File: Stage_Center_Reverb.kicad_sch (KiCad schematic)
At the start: 47 parts, among them J1 Input, J10 Power, J2 Output, J3 Tank, SW1a1 SW_SPDT, SW1c1 SW_SPDT, SW2 kill, U1 TL072, U10 L78L15, U11 L79L15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

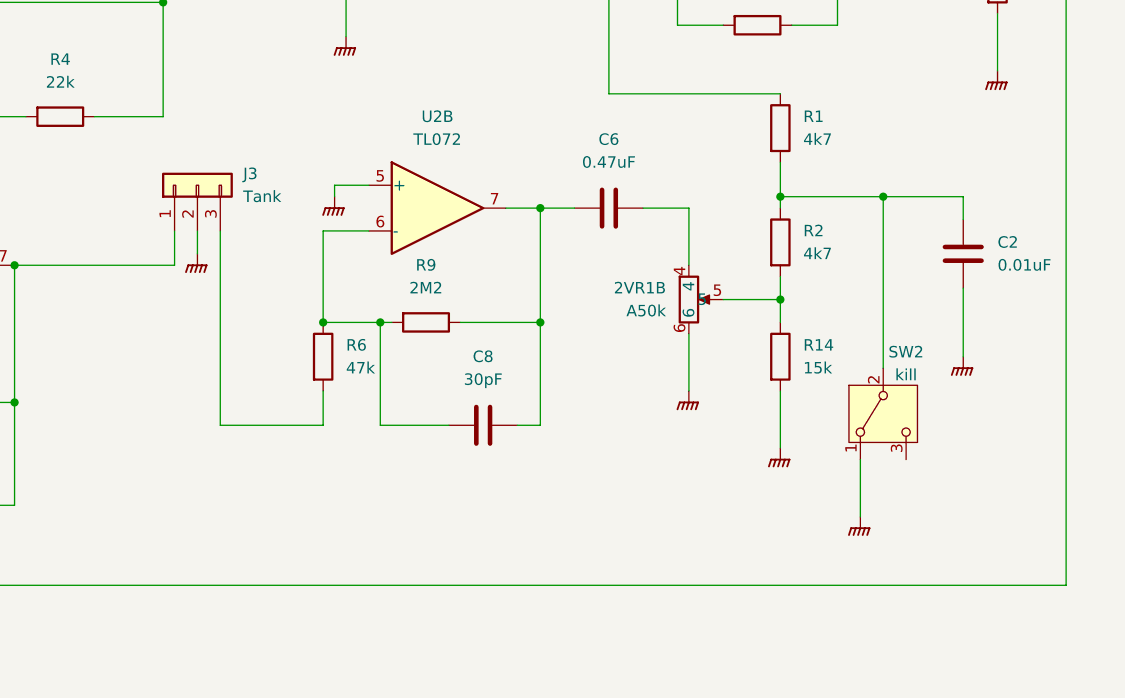
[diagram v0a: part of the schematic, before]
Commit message: 全体ではなく外周をGNDで囲むように変更
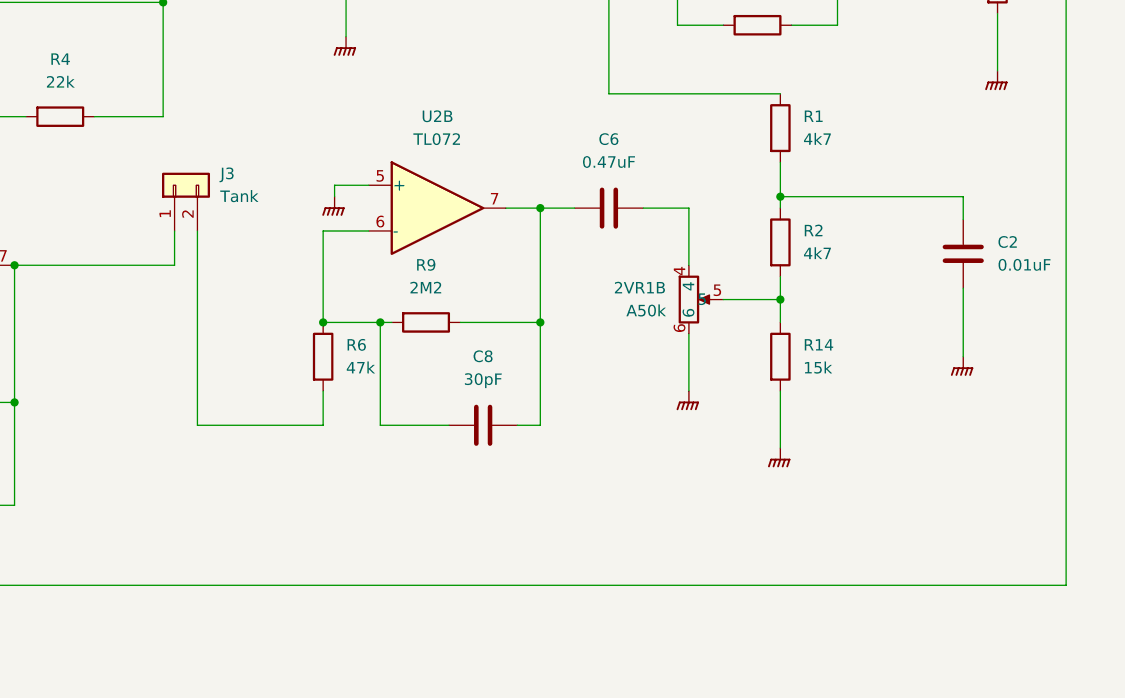
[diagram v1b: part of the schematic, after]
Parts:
- removed J3: Tank, Connector_JST:JST_XH_B3B-XH-A_1x03_P2.50mm_Vertical, symbol Connector_Generic:Conn_01x03
- removed SW2: kill, Connector_JST:JST_XH_B2B-XH-A_1x02_P2.50mm_Vertical, symbol Switch:SW_SPDT
- added J3: Tank, Connector_JST:JST_XH_B2B-XH-A_1x02_P2.50mm_Vertical, symbol Connector_Generic:Conn_01x02
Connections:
- net at R6.2: now also J3.2 (Pin_2)
- net at C1.2, U1.7, VR7.1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: now also J3.1 (Pin_1)
